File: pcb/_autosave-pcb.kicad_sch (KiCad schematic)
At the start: 219 parts, among them J2 Conn_01x04_Pin, J4 Conn_01x04_Socket, J5 Conn_01x02_Pin, Q1 BSS84, Q2 BSS84, Q3 BSS84, Q5 BSS84, SW1 SW_Push, SW10(8)1 SW_Push_45deg, SW11(9)1 SW_Push_45deg, SW12(0)1 SW_Push_45deg, SW13(-)1 SW_Push_45deg, SW14(=)1 SW_Push_45deg, SW15(bckspc)1 SW_Push_45deg, SW16(tab)1 SW_Push_45deg, SW17(q)1 SW_Push_45deg, SW18(w)1 SW_Push_45deg, SW19(e)1 SW_Push_45deg, SW2 SW_Push, SW2(esc)1 SW_Push_45deg, SW20(r)1 SW_Push_45deg, SW21(t)1 SW_Push_45deg, SW22(y)1 SW_Push_45deg, SW23(u)1 SW_Push_45deg, SW24(i)1 SW_Push_45deg, SW25(o)1 SW_Push_45deg, SW26(p)1 SW_Push_45deg, SW27([)1 SW_Push_45deg, SW28(])1 SW_Push_45deg, SW29(\)1 SW_Push_45deg, SW3 SW_Push, SW3(1)1 SW_Push_45deg, SW30(caps)1 SW_Push_45deg, SW31(unused)1 SW_Push_45deg, SW32(a)1 SW_Push_45deg, SW33(lshift)1 SW_Push_45deg, SW34(s)1 SW_Push_45deg, SW35(z)1 SW_Push_45deg, SW36(d)1 SW_Push_45deg, SW37(x)1 SW_Push_45deg, SW38(f)1 SW_Push_45deg, SW39(c)1 SW_Push_45deg, SW4 SW_Push, SW4(2)1 SW_Push_45deg, SW40(g)1 SW_Push_45deg, SW41(v)1 SW_Push_45deg, SW42(h)1 SW_Push_45deg, SW43(b)1 SW_Push_45deg, SW44(j)1 SW_Push_45deg, SW45(n)1 SW_Push_45deg, SW46(k)1 SW_Push_45deg, SW47(m)1 SW_Push_45deg, SW48(l)1 SW_Push_45deg, SW49(,)1 SW_Push_45deg, SW5 RS601A-1020013BB, SW5(3)1 SW_Push_45deg, SW50(;)1 SW_Push_45deg, SW51(.)1 SW_Push_45deg, SW52(')1 SW_Push_45deg, SW53(/)1 SW_Push_45deg, SW54(ret)1 SW_Push_45deg, SW55(rshift)1 SW_Push_45deg, SW56(unused)1 SW_Push_45deg, SW57(up)1 SW_Push_45deg, SW58(globe)1 SW_Push_45deg, SW6(4)1 SW_Push_45deg, SW60(lctrl)1 SW_Push_45deg, SW62(super)1 SW_Push_45deg, SW64(lalt)1 SW_Push_45deg, SW66(spc)1 SW_Push_45deg, SW68(spc)1 SW_Push_45deg, SW7(5)1 SW_Push_45deg, SW70(spc)1 SW_Push_45deg, SW72(spc)1 SW_Push_45deg, SW74(spc)1 SW_Push_45deg, SW76(ralt)1 SW_Push_45deg, SW78(rctrl)1 SW_Push_45deg, SW8(6)1 SW_Push_45deg, SW80(left)1 SW_Push_45deg, SW82(down)1 SW_Push_45deg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

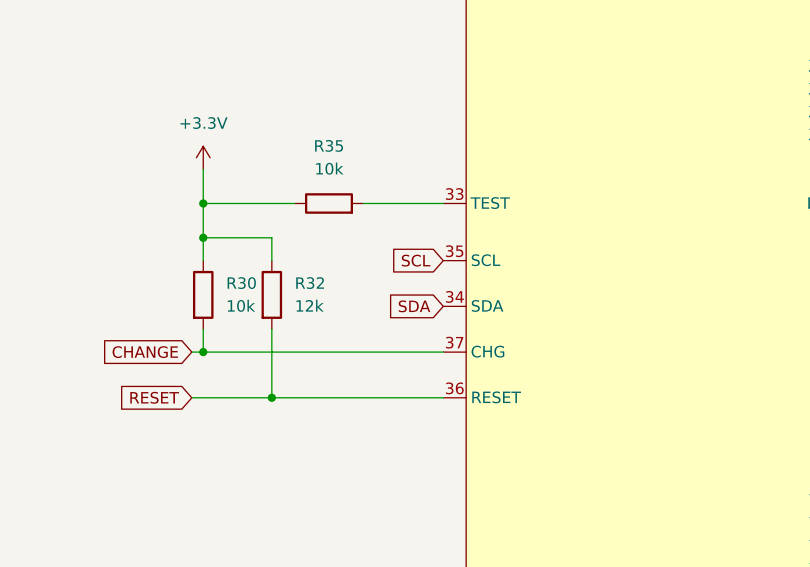
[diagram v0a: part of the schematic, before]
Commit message: make a hat attatchement
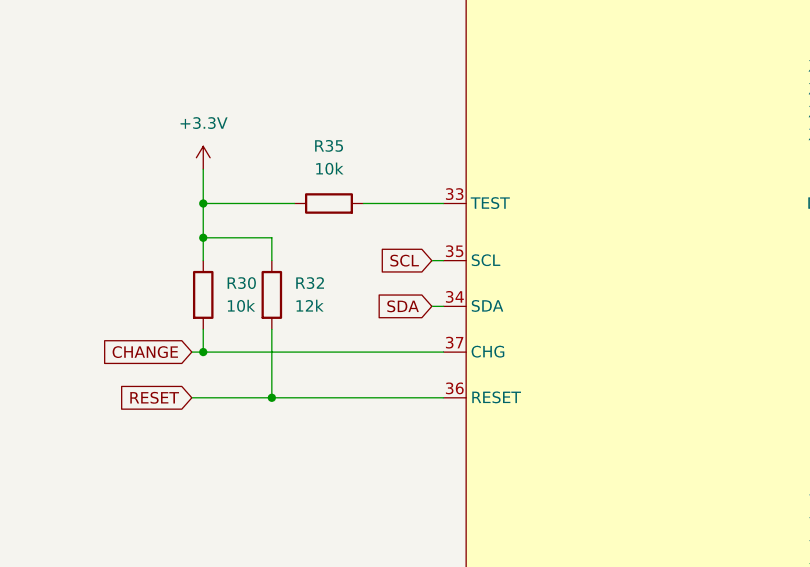
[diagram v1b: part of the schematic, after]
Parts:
- C10, C11, C12, C13, C14, C15, C16, C17, C18, C19, C6, C7, C8, C9: footprint (none) -> Capacitor_SMD:C_0603_1608Metric_Pad1.08x0.95mm_HandSolder
- H1, H2, H3, H4: footprint (none) -> MountingHole:MountingHole_3.2mm_M3_Pad_Via
- R30, R32, R35, R36: footprint (none) -> Capacitor_SMD:C_0805_2012Metric
- mXT336UD-MAU1: footprint MaxTouch:QFN-56_EP_6x6_Pitch0.35mm -> library:Touch IC
